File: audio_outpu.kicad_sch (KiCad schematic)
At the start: 33 parts, among them J2 NCJ6FA-H-0, J6 NCJ6FA-H-0, U5 OPA1656ID, U6 THAT1646, U7 THAT1646

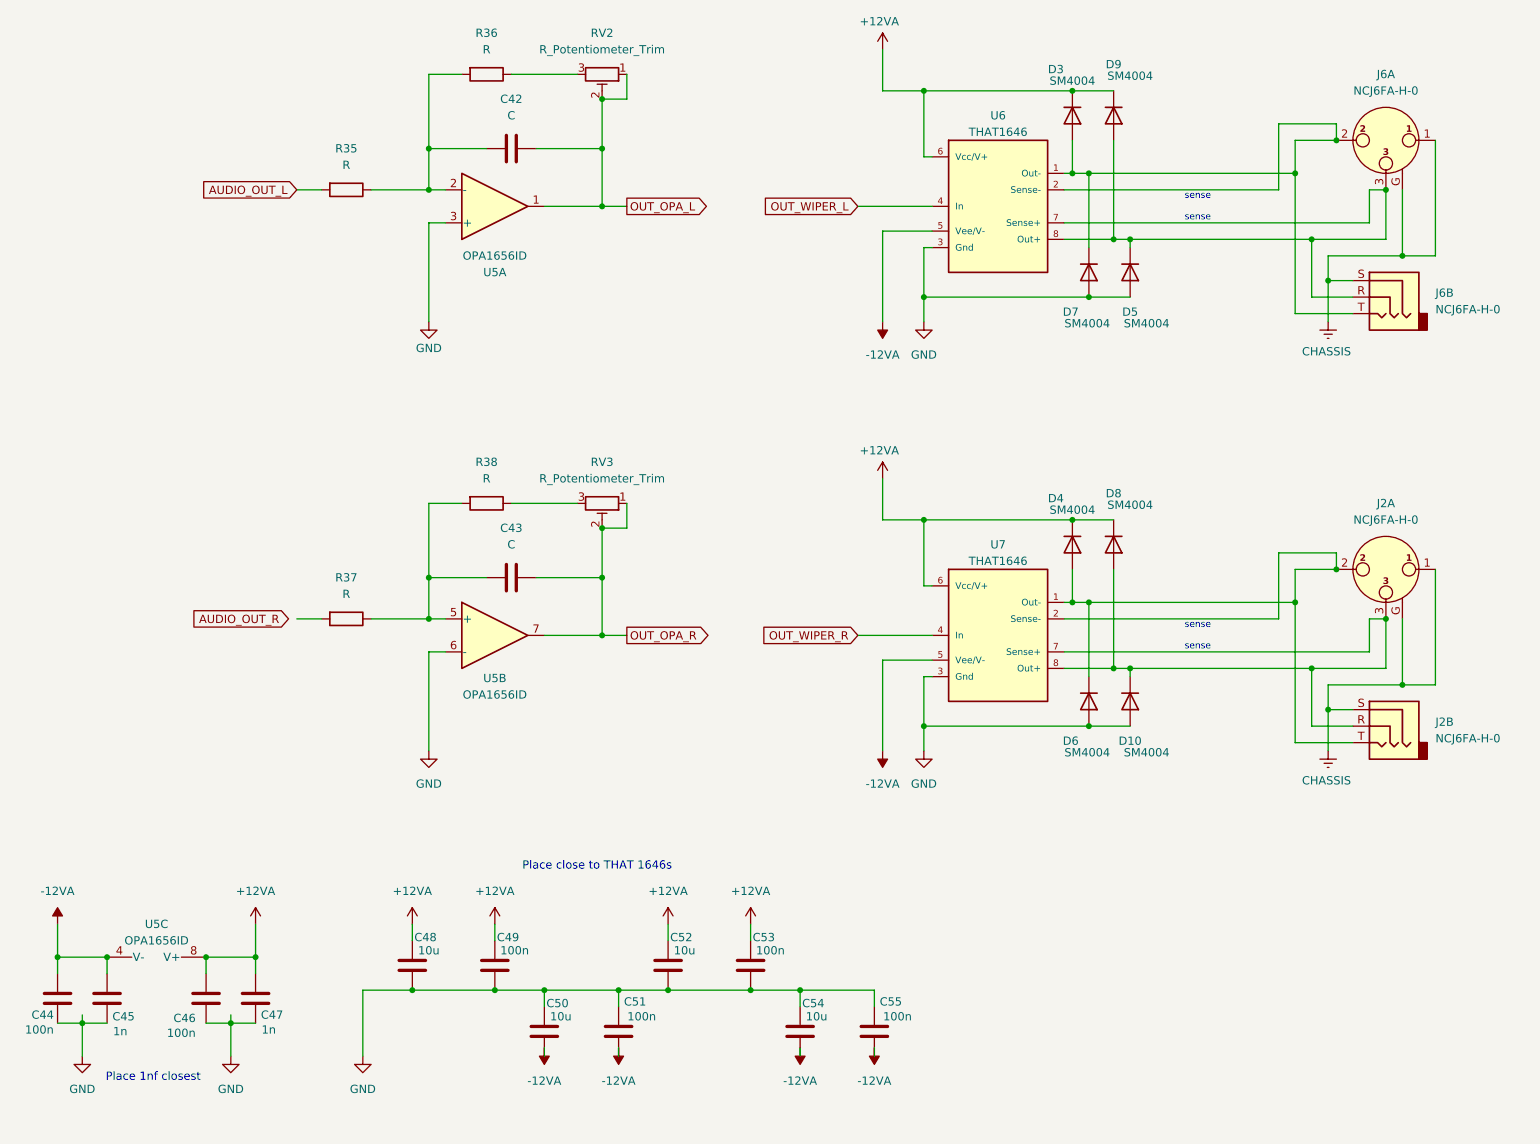
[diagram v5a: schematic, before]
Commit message: daughterboard added
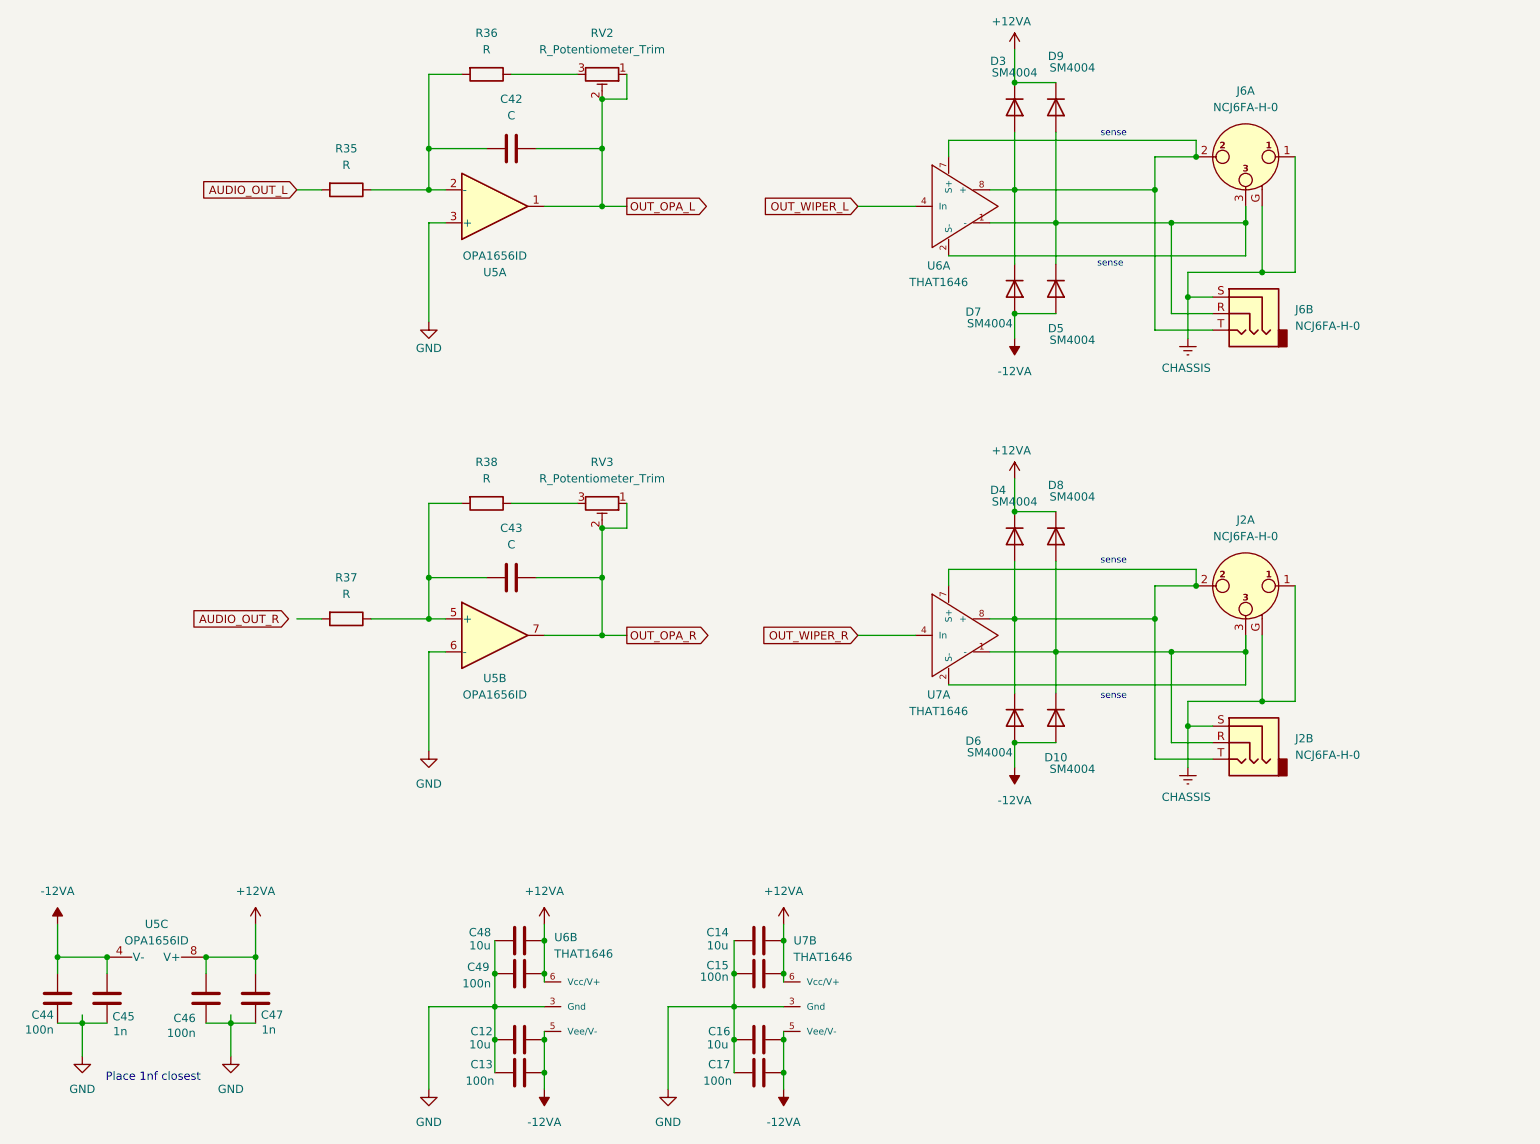
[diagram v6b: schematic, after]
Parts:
- removed C50, C52, C54: 10u, Capacitor_SMD:C_0805_2012Metric, symbol Device:C
- removed C51, C53, C55: 100n, Capacitor_SMD:C_0805_2012Metric, symbol Device:C
- added C12, C14, C16: 10u, Capacitor_SMD:C_0805_2012Metric, symbol Device:C
- added C13, C15, C17: 100n, Capacitor_SMD:C_0805_2012Metric, symbol Device:C
- added unit 3 of U5
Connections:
- net +12VA: now also C49.2, C14.1, C15.2, U5.8 (V+); no longer C49.1, U5.8 (V+)
- net -12VA: now also D10.2 (A), D5.2 (A), D6.2 (A), D7.2 (A), C12.1, C13.2, C16.1, C17.2, U5.4 (V-); no longer U5.4 (V-)
- net GND: now also C49.1, C12.2, C13.1, C14.2, C15.1, C16.2, C17.1; no longer C49.2, D10.2 (A), D5.2 (A), D6.2 (A), D7.2 (A)
- net at D3.2 (A), D7.1 (K), J6.2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: now also U6.7 (S+), U6.8 (+); no longer U6.1 (Out-), U6.2 (Sense-)
- net at D4.2 (A), D6.1 (K), J2.2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: now also U7.7 (S+), U7.8 (+); no longer U7.1 (Out-), U7.2 (Sense-)
- net at D10.1 (K), D8.2 (A), J2.3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: now also U7.1 (-), U7.2 (S-); no longer U7.7 (Sense+), U7.8 (Out+)
- net at D5.1 (K), D9.2 (A), J6.3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: now also U6.1 (-), U6.2 (S-); no longer U6.7 (Sense+), U6.8 (Out+)
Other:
- note removed: "Place close to THAT 1646s"
- moved on the sheet: C48, C49, D3, D5, D7, D9, J6A, J6B

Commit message: WIP trying to fix symbols and finish daughterboard
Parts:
- added unit 1 of U6
- added unit 1 of U7
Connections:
- net OUT_WIPER_L: now also U6.4 (In); no longer U6.4 (In)
- net OUT_WIPER_R: now also U7.4 (In); no longer U7.4 (In)
- net at D4.2 (A), D6.1 (K), J2.2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: now also U7.7 (S+), U7.8 (+); no longer U7.7 (S+), U7.8 (+)
- net at D3.2 (A), D7.1 (K), J6.2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: now also U6.7 (S+), U6.8 (+); no longer U6.7 (S+), U6.8 (+)
- net at D10.1 (K), D8.2 (A), J2.3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: now also U7.1 (-), U7.2 (S-); no longer U7.1 (-), U7.2 (S-)
- net at D5.1 (K), D9.2 (A), J6.3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: now also U6.1 (-), U6.2 (S-); no longer U6.1 (-), U6.2 (S-)

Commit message: All the testpoints
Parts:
- C16: renamed from C42; footprint (none) -> Capacitor_SMD:C_0805_2012Metric
- C17: renamed from C43; footprint (none) -> Capacitor_SMD:C_0805_2012Metric
- R19: renamed from R35; footprint (none) -> Resistor_SMD:R_0805_2012Metric
- R20: renamed from R37; footprint (none) -> Resistor_SMD:R_0805_2012Metric
- R21: renamed from R36; footprint (none) -> Resistor_SMD:R_0805_2012Metric
- R22: renamed from R38; footprint (none) -> Resistor_SMD:R_0805_2012Metric
- renumbered C44 to C12, C45 to C13, C46 to C14, C47 to C15, C48 to C18, C49 to C19, C12 to C20, C13 to C21, C14 to C22, C15 to C23, C16 to C24, C17 to C25, D7 to D4, D4 to D5, D9 to D7, D5 to D8, D8 to D9, J6 to J8, J2 to J9, RV2 to RV1, RV3 to RV2
